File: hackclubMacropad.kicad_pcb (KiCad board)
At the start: 2 copper layers, 70.5 x 90 mm, 21 parts, among them SW1 SW_Push, SW10 RotaryEncoder_Switch_MP, SW2 SW_Push, SW3 SW_Push, SW4 SW_Push, SW5 SW_Push, SW6 SW_Push, SW7 SW_Push, SW8 SW_Push, SW9 SW_Push, U1 MOUDLE-SEEEDUINO-XIAO

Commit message: added some 3d models to footprints
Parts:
- SW1, SW2, SW3, SW4, SW5, SW6, SW7, SW8, SW9: footprint Button_Switch_Keyboard:SW_Cherry_MX_1.00u_PCB -> footprints2:SW_Cherry_MX_1.00u_PCB
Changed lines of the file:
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@@
 	(net 23 "unconnected-(U1-PA6_A10_D10_MOSI-Pad11)")
 	(net 24 "/Row 0")
-	(footprint "Button_Switch_Keyboard:SW_Cherry_MX_1.00u_PCB"
+	(footprint "footprints2:SW_Cherry_MX_1.00u_PCB"
 		(layer "F.Cu")
 		(at 143.5495 97)
@@
 		)
 		(embedded_fonts no)
-		(model "${KICAD9_3DMODEL_DIR}/Button_Switch_Keyboard.3dshapes/SW_Cherry_MX_1.00u_PCB.step"
+		(model "C:/Users/Anabelle/Downloads/cherry-mx-red-switch-1.snapshot.3/Cherry MX.STEP"
 			(offset
-				(xyz 0 0 0)
+				(xyz -2.5 -4 0)
 			)
 			(scale
@@
 			)
 			(rotate
-				(xyz 0 0 0)
+				(xyz -90 -0 -0)
 			)
 		)
 	)
-	(footprint "Button_Switch_Keyboard:SW_Cherry_MX_1.00u_PCB"
+	(footprint "footprints2:SW_Cherry_MX_1.00u_PCB"
 		(layer "F.Cu")
 		(at 143.6295 78)
@@
 		)
 		(embedded_fonts no)
-		(model "${KICAD9_3DMODEL_DIR}/Button_Switch_Keyboard.3dshapes/SW_Cherry_MX_1.00u_PCB.step"
+		(model "C:/Users/Anabelle/Downloads/cherry-mx-red-switch-1.snapshot.3/Cherry MX.STEP"
 			(offset
-				(xyz 0 0 0)
+				(xyz -2.5 -4 0)
 			)
 			(scale
@@
 			)
 			(rotate
-				(xyz 0 0 0)
+				(xyz -90 -0 -0)
 			)
 		)
 	)
-	(footprint "Button_Switch_Keyboard:SW_Cherry_MX_1.00u_PCB"
+	(footprint "footprints2:SW_Cherry_MX_1.00u_PCB"
 		(layer "F.Cu")
 		(at 162.5495 116)
@@
 		)
 		(embedded_fonts no)
-		(model "${KICAD9_3DMODEL_DIR}/Button_Switch_Keyboard.3dshapes/SW_Cherry_MX_1.00u_PCB.step"
+		(model "C:/Users/Anabelle/Downloads/cherry-mx-red-switch-1.snapshot.3/Cherry MX.STEP"
 			(offset
-				(xyz 0 0 0)
+				(xyz -2.5 -4 0)
 			)
 			(scale
@@
 			)
 			(rotate
-				(xyz 0 0 0)
+				(xyz -90 -0 -0)
 			)
 		)
 	)
-	(footprint "Button_Switch_Keyboard:SW_Cherry_MX_1.00u_PCB"
+	(footprint "footprints2:SW_Cherry_MX_1.00u_PCB"
 		(layer "F.Cu")
 		(at 124.5495 116)
@@
 		)
 		(embedded_fonts no)
-		(model "${KICAD9_3DMODEL_DIR}/Button_Switch_Keyboard.3dshapes/SW_Cherry_MX_1.00u_PCB.step"
+		(model "C:/Users/Anabelle/Downloads/cherry-mx-red-switch-1.snapshot.3/Cherry MX.STEP"
 			(offset
-				(xyz 0 0 0)
+				(xyz -2.5 -4 0)
 			)
 			(scale
@@
 			)
 			(rotate
-				(xyz 0 0 0)
+				(xyz -90 -0 -0)
 			)
 		)
 	)
-	(footprint "Button_Switch_Keyboard:SW_Cherry_MX_1.00u_PCB"
+	(footprint "footprints2:SW_Cherry_MX_1.00u_PCB"
 		(layer "F.Cu")
 		(at 124.6295 78)
@@
 		)
 		(embedded_fonts no)
-		(model "${KICAD9_3DMODEL_DIR}/Button_Switch_Keyboard.3dshapes/SW_Cherry_MX_1.00u_PCB.step"
+		(model "C:/Users/Anabelle/Downloads/cherry-mx-red-switch-1.snapshot.3/Cherry MX.STEP"
 			(offset
-				(xyz 0 0 0)
+				(xyz -2.5 -4 0)
 			)
 			(scale
@@
 			)
 			(rotate
-				(xyz 0 0 0)
+				(xyz -90 -0 -0)
 			)
 		)
 	)
-	(footprint "Button_Switch_Keyboard:SW_Cherry_MX_1.00u_PCB"
+	(footprint "footprints2:SW_Cherry_MX_1.00u_PCB"
 		(layer "F.Cu")
 		(at 162.6295 97)
@@
 		)
 		(embedded_fonts no)
-		(model "${KICAD9_3DMODEL_DIR}/Button_Switch_Keyboard.3dshapes/SW_Cherry_MX_1.00u_PCB.step"
+		(model "C:/Users/Anabelle/Downloads/cherry-mx-red-switch-1.snapshot.3/Cherry MX.STEP"
 			(offset
-				(xyz 0 0 0)
+				(xyz -2.5 -4 0)
 			)
 			(scale
@@
 			)
 			(rotate
-				(xyz 0 0 0)
+				(xyz -90 -0 -0)
 			)
 		)
 	)
-	(footprint "Button_Switch_Keyboard:SW_Cherry_MX_1.00u_PCB"
+	(footprint "footprints2:SW_Cherry_MX_1.00u_PCB"
 		(layer "F.Cu")
 		(at 124.6295 97)
@@
 		)
 		(embedded_fonts no)
-		(model "${KICAD9_3DMODEL_DIR}/Button_Switch_Keyboard.3dshapes/SW_Cherry_MX_1.00u_PCB.step"
+		(model "C:/Users/Anabelle/Downloads/cherry-mx-red-switch-1.snapshot.3/Cherry MX.STEP"
 			(offset
-				(xyz 0 0 0)
+				(xyz -2.5 -4 0)
 			)
 			(scale
@@
 			)
 			(rotate
-				(xyz 0 0 0)
+				(xyz -90 -0 -0)
 			)
 		)
@@
 		)
 	)
-	(footprint "Button_Switch_Keyboard:SW_Cherry_MX_1.00u_PCB"
+	(footprint "footprints2:SW_Cherry_MX_1.00u_PCB"
 		(layer "F.Cu")
 		(at 162.6295 78)
@@
 		)
 		(embedded_fonts no)
-		(model "${KICAD9_3DMODEL_DIR}/Button_Switch_Keyboard.3dshapes/SW_Cherry_MX_1.00u_PCB.step"
+		(model "C:/Users/Anabelle/Downloads/cherry-mx-red-switch-1.snapshot.3/Cherry MX.STEP"
 			(offset
-				(xyz 0 0 0)
+				(xyz -2.5 -4 0)
 			)
 			(scale
@@
 			)
 			(rotate
-				(xyz 0 0 0)
+				(xyz -90 -0 -0)
 			)
 		)
 	)
-	(footprint "Button_Switch_Keyboard:SW_Cherry_MX_1.00u_PCB"
+	(footprint "footprints2:SW_Cherry_MX_1.00u_PCB"
 		(layer "F.Cu")
 		(at 143.5495 116)
@@
 		)
 		(embedded_fonts no)
-		(model "${KICAD9_3DMODEL_DIR}/Button_Switch_Keyboard.3dshapes/SW_Cherry_MX_1.00u_PCB.step"
+		(model "C:/Users/Anabelle/Downloads/cherry-mx-red-switch-1.snapshot.3/Cherry MX.STEP"
 			(offset
-				(xyz 0 0 0)
+				(xyz -2.5 -4 0)
 			)
 			(scale
@@
 			)
 			(rotate
-				(xyz 0 0 0)
+				(xyz -90 -0 -0)
 			)
 		)
@@
 		)
 		(embedded_fonts no)
+		(model "C:/Users/Anabelle/Downloads/seeed-studio-xiao-rp2040-3d-model/Seeed Studio XIAO RP2040 v26.step"
+			(offset
+				(xyz 0 0 0)
+			)
+			(scale
+				(xyz 1 1 1)
+			)
+			(rotate
+				(xyz 0 0 0)
+			)
+		)
 	)
 	(footprint "Diode_THT:D_DO-35_SOD27_P7.62mm_Horizontal"

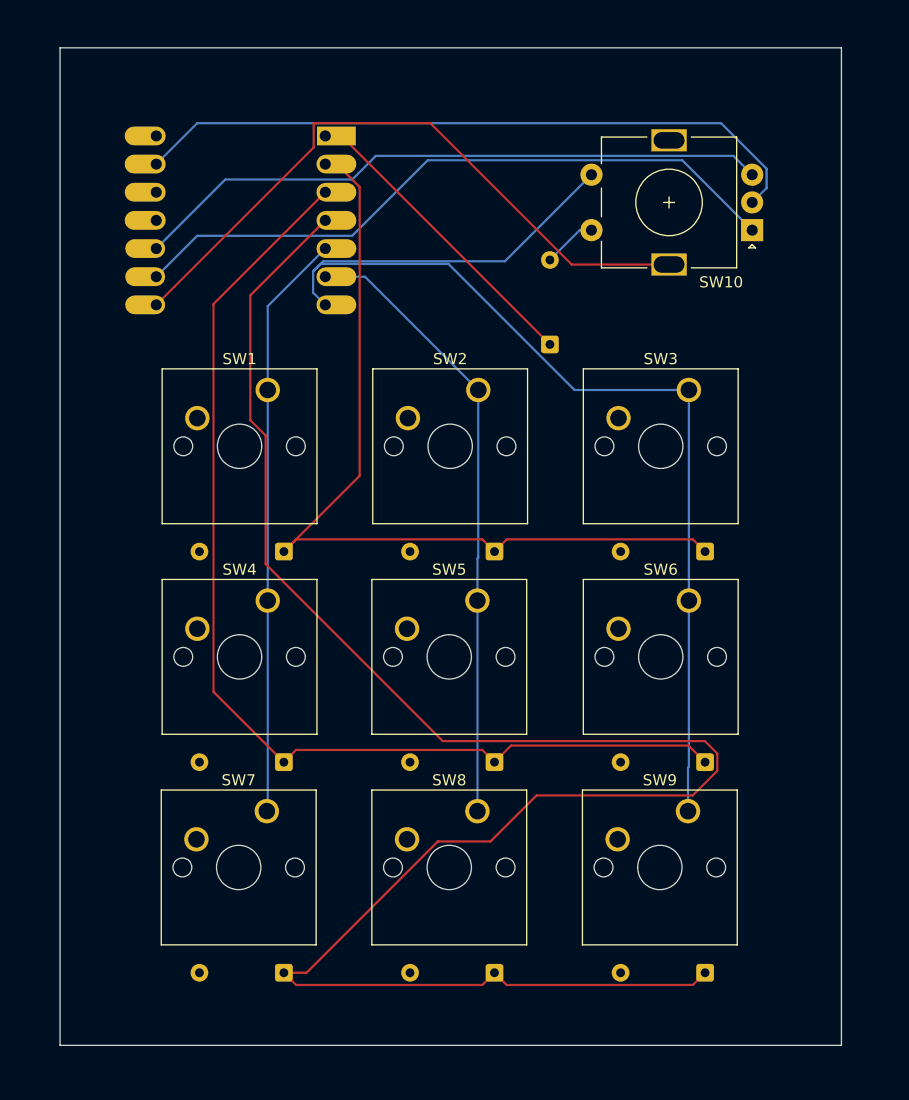
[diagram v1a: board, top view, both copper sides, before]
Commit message: added footprints
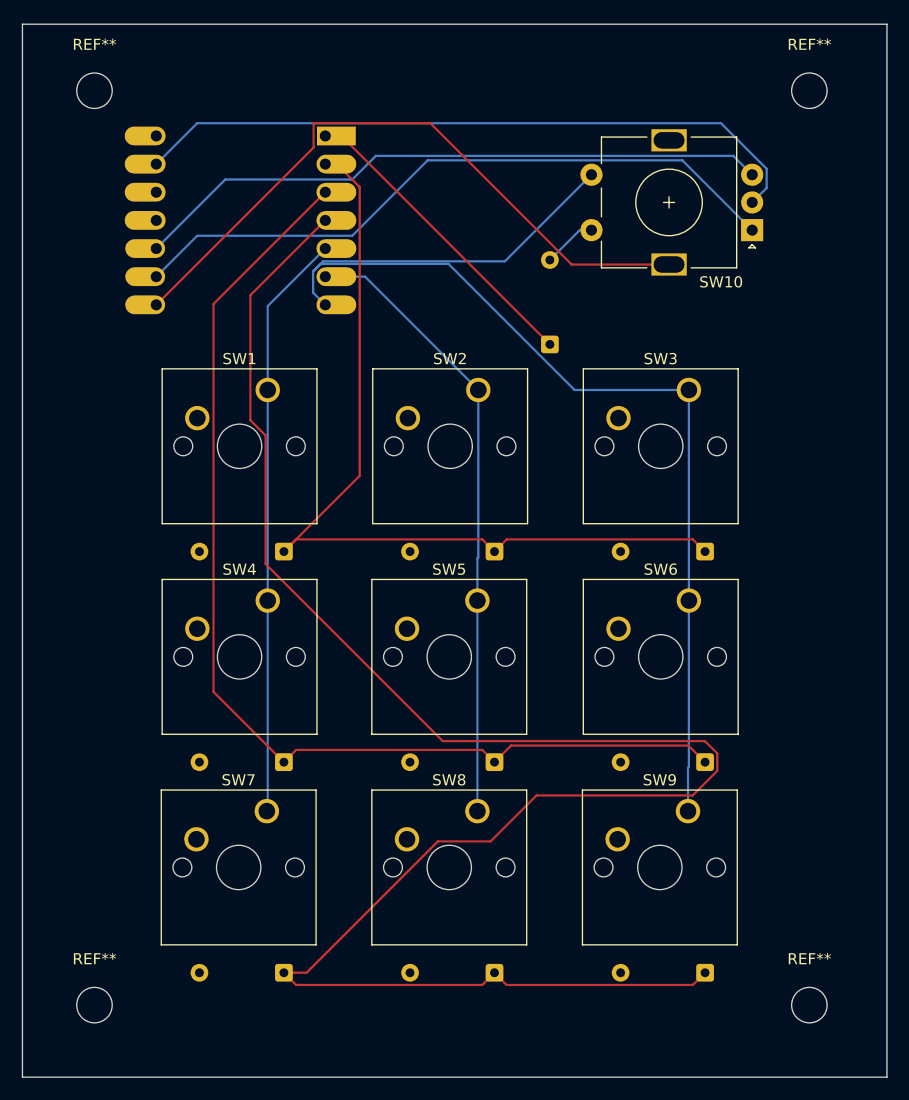
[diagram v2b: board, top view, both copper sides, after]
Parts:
- added REF**: MountingHole_3.2mm_M3, MountingHole:MountingHole_3.2mm_M3, F.Cu at (173.5, 133.5)
- added REF**: MountingHole_3.2mm_M3, MountingHole:MountingHole_3.2mm_M3, F.Cu at (109.0, 51.0)
- added REF**: MountingHole_3.2mm_M3, MountingHole:MountingHole_3.2mm_M3, F.Cu at (173.5, 51.0)
- added REF**: MountingHole_3.2mm_M3, MountingHole:MountingHole_3.2mm_M3, F.Cu at (109.0, 133.5)
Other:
- board size 70.5 x 90 mm -> 78 x 95 mm

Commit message: finished macropad case and assembly
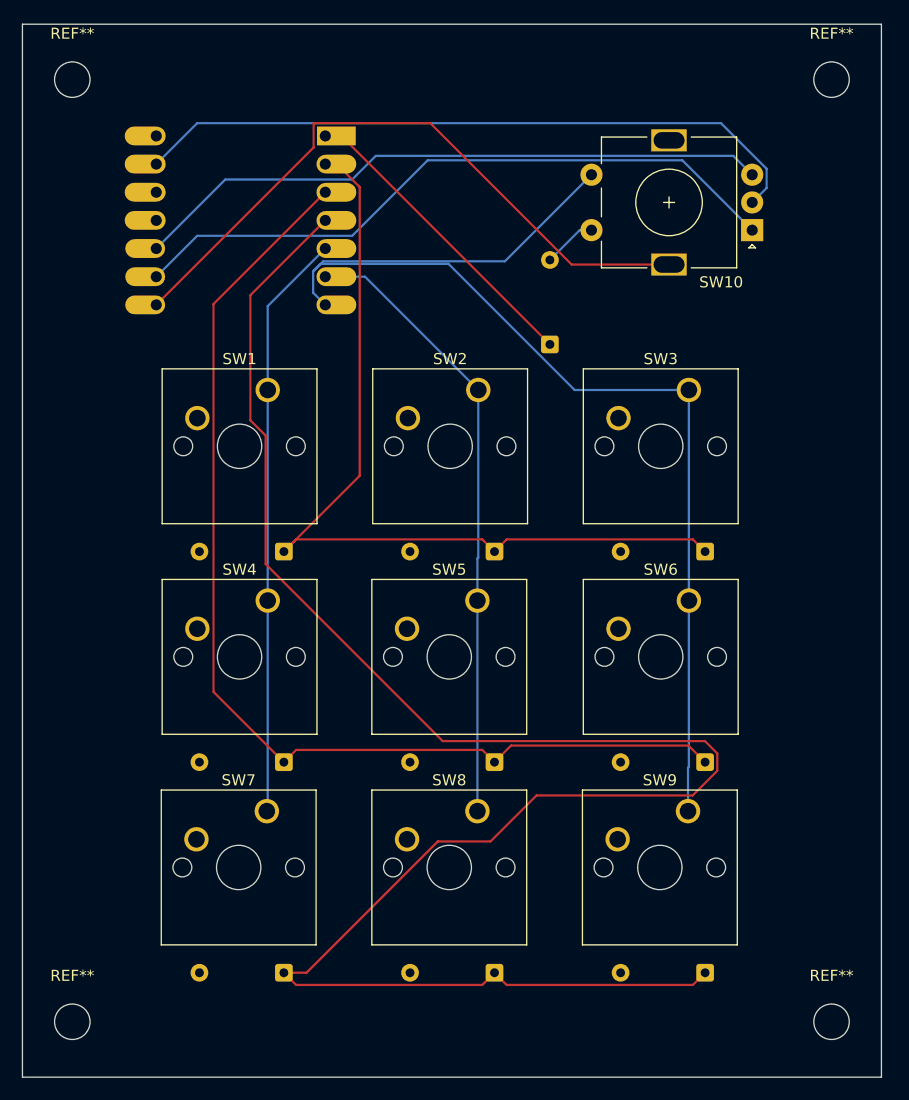
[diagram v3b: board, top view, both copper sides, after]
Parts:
- moved REF** 2.50 mm to (175.5, 135.0)
- moved REF** 2.50 mm to (107.0, 135.0)
- moved REF** 2.24 mm to (107.0, 50.0)
- moved REF** 2.24 mm to (175.5, 50.0)
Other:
- board size 78 x 95 mm -> 77.5 x 95 mm
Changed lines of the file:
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@@
 	)
 	(setup
+		(stackup
+			(layer "F.SilkS"
+				(type "Top Silk Screen")
+			)
+			(layer "F.Paste"
+				(type "Top Solder Paste")
+			)
+			(layer "F.Mask"
+				(type "Top Solder Mask")
+				(thickness 0.01)
+			)
+			(layer "F.Cu"
+				(type "copper")
+				(thickness 0.035)
+			)
+			(layer "dielectric 1"
+				(type "core")
+				(thickness 1.51)
+				(material "FR4")
+				(epsilon_r 4.5)
+				(loss_tangent 0.02)
+			)
+			(layer "B.Cu"
+				(type "copper")
+				(thickness 0.035)
+			)
+			(layer "B.Mask"
+				(type "Bottom Solder Mask")
+				(thickness 0.01)
+			)
+			(layer "B.Paste"
+				(type "Bottom Solder Paste")
+			)
+			(layer "B.SilkS"
+				(type "Bottom Silk Screen")
+			)
+			(copper_finish "None")
+			(dielectric_constraints no)
+		)
 		(pad_to_mask_clearance 0)
 		(allow_soldermask_bridges_in_footprints no)
@@
 	(footprint "MountingHole:MountingHole_3.2mm_M3"
 		(layer "F.Cu")
-		(at 173.5 133.5)
+		(at 175.5 135)
 		(descr "Mounting Hole 3.2mm, M3, no annular, generated by kicad-footprint-generator mountinghole.py")
 		(tags "mountinghole M3")
@@
 	(footprint "MountingHole:MountingHole_3.2mm_M3"
 		(layer "F.Cu")
-		(at 109 51)
+		(at 107 50)
 		(descr "Mounting Hole 3.2mm, M3, no annular, generated by kicad-footprint-generator mountinghole.py")
 		(tags "mountinghole M3")
@@
 	(footprint "MountingHole:MountingHole_3.2mm_M3"
 		(layer "F.Cu")
-		(at 173.5 51)
+		(at 175.5 50)
 		(descr "Mounting Hole 3.2mm, M3, no annular, generated by kicad-footprint-generator mountinghole.py")
 		(tags "mountinghole M3")
@@
 	(footprint "MountingHole:MountingHole_3.2mm_M3"
 		(layer "F.Cu")
-		(at 109 133.5)
+		(at 107 135)
 		(descr "Mounting Hole 3.2mm, M3, no annular, generated by kicad-footprint-generator mountinghole.py")
 		(tags "mountinghole M3")
@@
 	(gr_rect
 		(start 102.5 45)
-		(end 180.5 140)
+		(end 180 140)
 		(stroke
 			(width 0.05)
